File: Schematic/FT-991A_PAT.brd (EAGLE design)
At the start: 44.6 x 59.8 mm, 32 parts, among them Q2 MC78L09ABDR2GOSCT, Q5 NCP553, Q7 J310, Q8 5086, X1 IF_IN, X2 SCP_OUT, X3 SDR_OUT

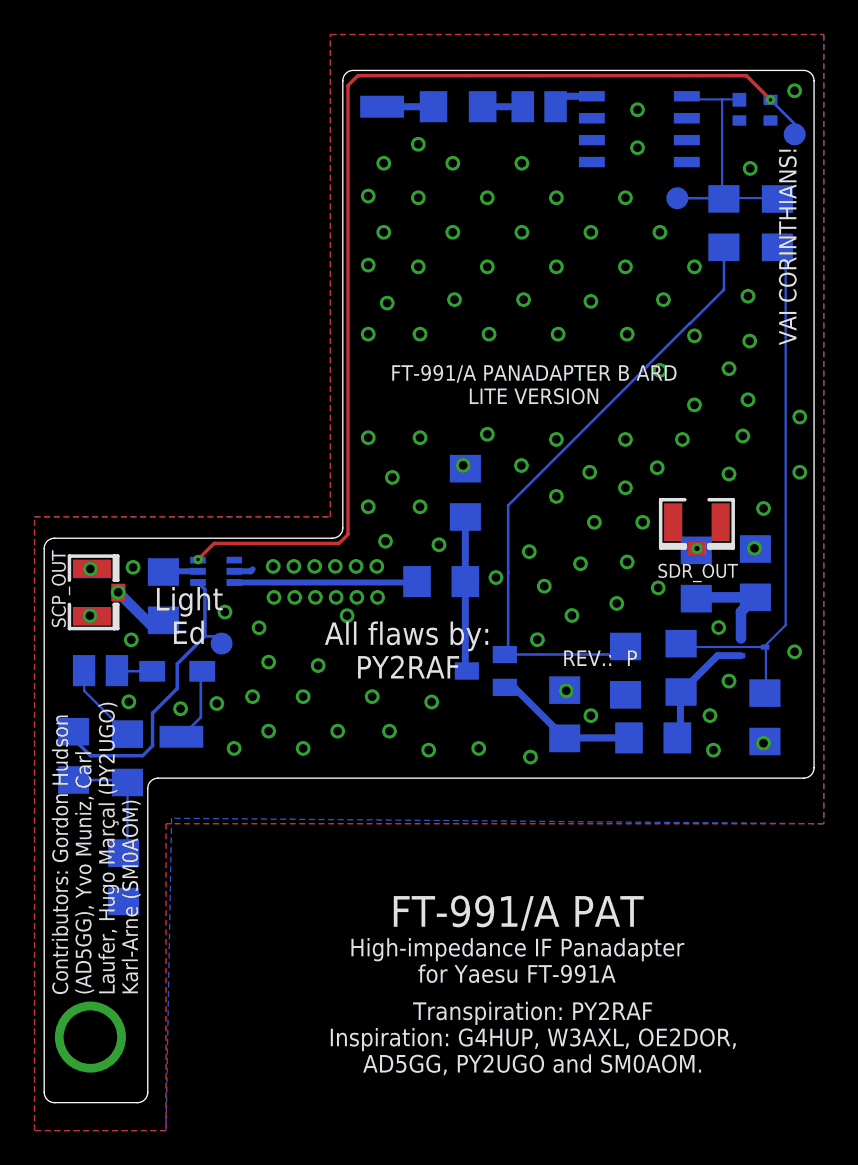
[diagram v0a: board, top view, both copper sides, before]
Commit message: Preparing: Revision Q
* Better Silk-Screen Pin 1 markings for Power regulators
* Larger footprint for 2SC5086
* Moving 0.1µF transistor caps away from RF section
* Lots of re-routing
* Changing 1 nF caps to Low ESL type and 0805 footprint for better RF
  performance
* Labeled a few signals in Eagle file for better understanding of signal
  route/path
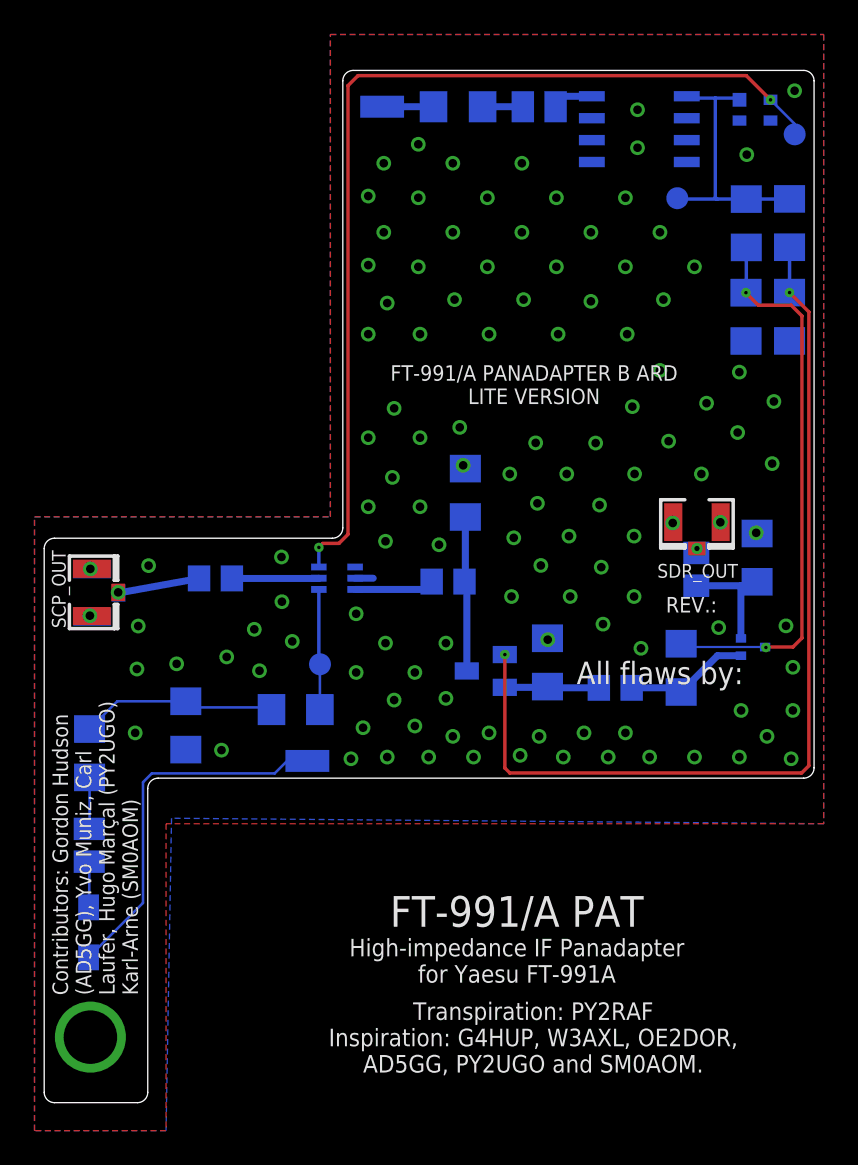
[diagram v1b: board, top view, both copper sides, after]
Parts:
- C1, C10, C13, C6: value 1nF -> 1000pF; device rcl:C3216 -> rcl:C0805
- Q1: value (none) -> PE4259
- moved C11 23.2 mm to (47.0, 57.1)
- moved C7 22.6 mm to (49.5, 57.1)
- moved D1 16.0 mm to (8.90, 21.5), turned to 270 degrees
- moved R2 13.1 mm to (20.9, 34.4), turned to 180 degrees
- moved L3 10.1 mm to (8.93, 26.5), turned to 90 degrees
- moved R4 9.51 mm to (14.5, 33.5)
- moved PAD3 7.43 mm to (21.6, 31.4)
- moved Q1 7.01 mm to (23.3, 42.0)
- moved TP3 5.82 mm to (22.3, 37.0)
- moved R6 3.80 mm to (49.5, 62.6)
- moved C10 3.64 mm to (39.4, 35.6)
- moved C1 3.19 mm to (16.2, 42.0), turned to 180 degrees
- moved R7 3.16 mm to (35.5, 37.1)
- moved R3 2.22 mm to (8.95, 31.8), turned to 270 degrees
- moved R9 1.80 mm to (47.0, 62.5)
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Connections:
- net N$10 renamed 9V5086
- net N$2 renamed IFTAP
- net N$3 renamed IFIN
- net N$37 renamed FINAL
- net N$9 renamed 9VJ310
- net VCC renamed 9V
- net VDD renamed 3V
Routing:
- net 9VJ310: track 36.1 -> 55.0 mm, vias 0 -> 2
- net N$18: track 4.30 -> 21.5 mm
- net N$7: track 17.7 -> 6.99 mm
- net 3V: track 63.2 -> 57.0 mm
- net IFIN: track 10.6 -> 4.63 mm
- net N$8: track 7.48 -> 11.6 mm
- net IFTAP: track 2.02 -> 5.05 mm
- net N$5: track 8.45 -> 5.49 mm
- net N$25: track 4.72 -> 2.99 mm
- net N$27: track 3.58 -> 4.74 mm
- net 9V5086: track 31.6 -> 32.4 mm, vias 0 -> 2
- net 9V: track 14.8 -> 15.6 mm
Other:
- board text added: "All flaws by:"
- board text added: "PY2RAF"
- board text removed: "All flaws by: PY2RAF"

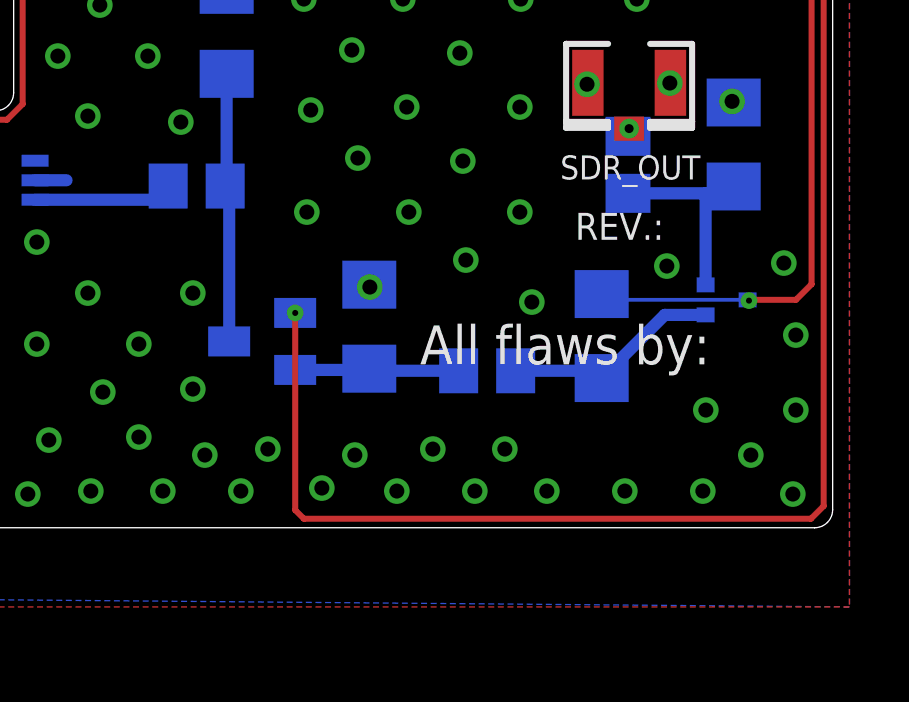
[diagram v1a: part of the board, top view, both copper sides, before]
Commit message: Minor routing hacks
- Replaced J310 JFET
  * Taking full advantage of its Source and Drain interchangeability
  * Avoiding some signal track xing
- And more routing changes.
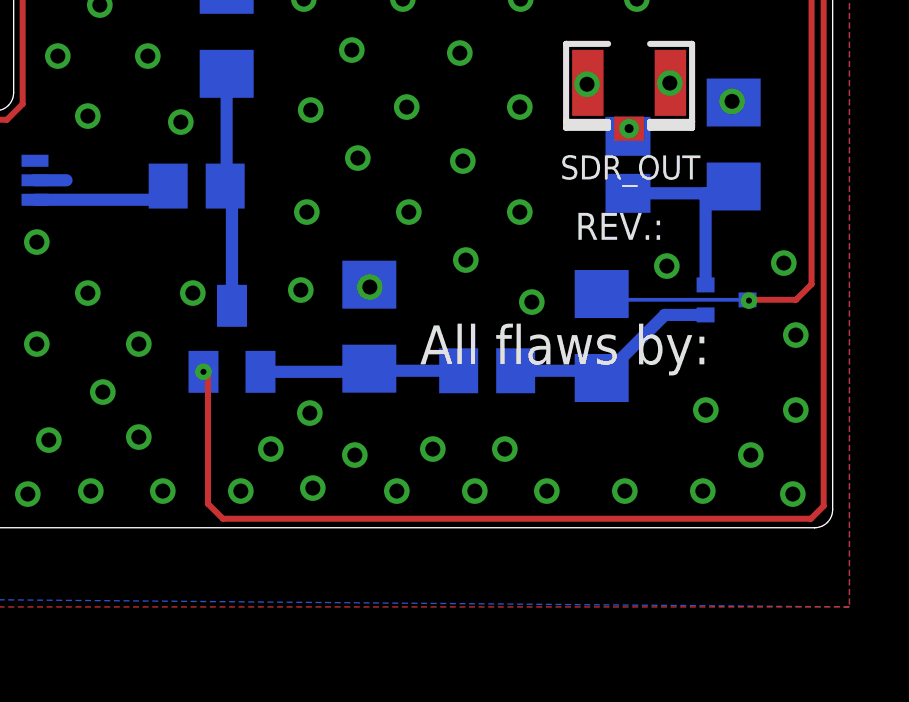
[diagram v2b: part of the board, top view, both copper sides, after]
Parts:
- Q7: device transistor-fet:SOT23 -> aarf:SOT23-3
- moved Q7 1.01 mm to (30.9, 36.7), turned to 0 degrees
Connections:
- net N$27 renamed RAWIN
- net 9VJ310: now also Q7.2; no longer Q7.1
- net N$5: now also Q7.1; no longer Q7.2
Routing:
- net N$5: track 5.49 -> 6.68 mm
- net N$6: track 9.00 -> 7.85 mm
- net 9VJ310: track 55.0 -> 55.9 mm
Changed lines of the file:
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@@
 <drawing>
 <settings>
-<setting alwaysvectorfont="no"/>
+<setting alwaysvectorfont="yes"/>
 <setting keepoldvectorfont="yes"/>
 <setting verticaltext="up"/>
@@
 <attribute name="VALUE" x="43.8775" y="57.1275" size="0.8" layer="22" font="vector" ratio="15" rot="MR270" align="top-center"/>
 </element>
-<element name="Q7" library="transistor-fet" library_urn="urn:adsk.eagle:library:396" package="SOT23" package3d_urn="urn:adsk.eagle:package:28534/2" value="J310" x="31.9075" y="36.612815625" smashed="yes" rot="MR270">
-<attribute name="SPICEPREFIX" value="J" x="31.9075" y="36.612815625" size="1.778" layer="28" rot="MR270" display="off"/>
-<attribute name="VALUE" x="31.9075" y="33.907815625" size="0.8" layer="22" font="vector" ratio="15" rot="MR180" align="top-center"/>
-</element>
 <element name="Q8" library="aarf" package="2-2H1A" value="5086" x="47.3875" y="37.9975" smashed="yes" rot="MR90">
 <attribute name="VALUE" x="47.2025" y="36.2875" size="0.8" layer="22" font="vector" ratio="15" rot="MR0" align="center"/>
@@
 <attribute name="TP_SIGNAL_NAME" value="" x="22.3" y="37" size="1.778" layer="28" rot="MR0" display="off"/>
 <attribute name="VALUE" x="22.935" y="36.238" size="0.0254" layer="28" rot="MR0"/>
+</element>
+<element name="Q7" library="aarf" package="SOT23-3" value="J310" x="30.9" y="36.7" smashed="yes" rot="MR0">
+<attribute name="VALUE" x="30.905" y="34.225" size="0.8" layer="22" font="vector" ratio="15" rot="MR0" align="center"/>
 </element>
 </elements>
@@
 <contactref element="R7" pad="2"/>
 <contactref element="C10" pad="1"/>
-<contactref element="Q7" pad="2"/>
-<wire x1="33.0075" y1="35.662815625" x2="35.435315625" y2="35.662815625" width="0.4064" layer="16"/>
-<wire x1="35.435315625" y1="35.662815625" x2="35.4775" y2="35.705" width="0.4064" layer="16"/>
+<contactref element="Q7" pad="1"/>
+<wire x1="31.85" y1="35.6" x2="35.3725" y2="35.6" width="0.4064" layer="16"/>
+<wire x1="35.3725" y1="35.6" x2="35.4775" y2="35.705" width="0.4064" layer="16"/>
 <wire x1="35.4775" y1="35.705" x2="35.5475" y2="35.635" width="0.4064" layer="16"/>
 <wire x1="35.5475" y1="35.635" x2="38.455" y2="35.635" width="0.4064" layer="16"/>
 </signal>
 <signal name="N$6">
-<contactref element="Q7" pad="3"/>
 <contactref element="R5" pad="2"/>
 <contactref element="C6" pad="2"/>
-<wire x1="30.8075" y1="41.655409375" x2="30.67225625" y2="41.790653125" width="0.4064" layer="16"/>
-<wire x1="30.8075" y1="36.612815625" x2="30.8075" y2="41.655409375" width="0.4064" layer="16"/>
 <wire x1="30.7225" y1="45.5325" x2="30.7225" y2="41.840896875" width="0.4064" layer="16"/>
 <wire x1="30.7225" y1="41.840896875" x2="30.67225625" y2="41.790653125" width="0.4064" layer="16"/>
+<contactref element="Q7" pad="3"/>
+<wire x1="30.9" y1="37.8" x2="30.9" y2="41.562909375" width="0.4064" layer="16"/>
+<wire x1="30.9" y1="41.562909375" x2="30.67225625" y2="41.790653125" width="0.4064" layer="16"/>
 </signal>
 <signal name="GNDA" airwireshidden="yes">
@@
 <via x="26.595" y="34.925" extent="1-16" drill="0.5"/>
 <via x="24.395" y="36.525" extent="1-16" drill="0.5"/>
-<via x="29.595" y="35.025" extent="1-16" drill="0.5"/>
+<via x="33.195" y="38.325" extent="1-16" drill="0.5"/>
 <via x="24.795" y="33.325" extent="1-16" drill="0.5"/>
 <via x="24.095" y="31.525" extent="1-16" drill="0.5"/>
@@
 <via x="38.995" y="31.625" extent="1-16" drill="0.5"/>
 <via x="36.395" y="31.625" extent="1-16" drill="0.5"/>
-<via x="32.095" y="33.025" extent="1-16" drill="0.5"/>
+<via x="32.195" y="33.025" extent="1-16" drill="0.5"/>
 <via x="31.195" y="31.625" extent="1-16" drill="0.5"/>
 <via x="28.595" y="31.625" extent="1-16" drill="0.5"/>
@@
 <via x="37.595" y="33.025" extent="1-16" drill="0.5"/>
 <via x="34.995" y="32.825" extent="1-16" drill="0.5"/>
-<via x="33.895" y="31.725" extent="1-16" drill="0.5"/>
-<via x="29.995" y="32.825" extent="1-16" drill="0.5"/>
+<via x="33.595" y="31.725" extent="1-16" drill="0.5"/>
+<via x="33.495" y="34.225" extent="1-16" drill="0.5"/>
 <via x="27.795" y="33.425" extent="1-16" drill="0.5"/>
 <via x="39.995" y="33.025" extent="1-16" drill="0.5"/>
@@
 <signal name="9VJ310">
 <contactref element="R6" pad="1"/>
-<contactref element="Q7" pad="1"/>
 <contactref element="C7" pad="1"/>
-<wire x1="33" y1="37.570315625" x2="33.0075" y2="37.562815625" width="0.2" layer="16"/>
 <via x="49.5025" y="58.5325" extent="1-16" drill="0.2"/>
 <wire x1="49.5025" y1="58.5325" x2="50.6225" y2="57.4125" width="0.2" layer="1"/>
-<wire x1="50.2" y1="30.7025" x2="50.6225" y2="31.125" width="0.2" layer="1"/>
+<wire x1="50.6225" y1="31.125" x2="50.2" y2="30.7025" width="0.2" layer="1"/>
 <wire x1="50.6225" y1="57.4125" x2="50.6225" y2="31.125" width="0.2" layer="1"/>
-<via x="33.0075" y="37.562815625" extent="1-16" drill="0.2"/>
-<wire x1="33.0075" y1="37.562815625" x2="33.0075" y2="30.9925" width="0.2" layer="1"/>
-<wire x1="33.0075" y1="30.9925" x2="33.2975" y2="30.7025" width="0.2" layer="1"/>
-<wire x1="33.2975" y1="30.7025" x2="50.2" y2="30.7025" width="0.2" layer="1"/>
 <wire x1="49.5025" y1="61.16" x2="49.5025" y2="58.5325" width="0.2" layer="16"/>
+<contactref element="Q7" pad="2"/>
+<wire x1="30.5975" y1="30.7025" x2="50.2" y2="30.7025" width="0.2" layer="1"/>
+<wire x1="30.5975" y1="30.7025" x2="30.1" y2="31.2" width="0.2" layer="1"/>
+<wire x1="30.1" y1="31.2" x2="30.1" y2="33.9" width="0.2" layer="1"/>
+<wire x1="30.1" y1="33.9" x2="30.1" y2="34.05" width="0.2" layer="1"/>
+<wire x1="30.1" y1="34.05" x2="30.1" y2="35.45" width="0.2" layer="1"/>
+<wire x1="30.1" y1="35.45" x2="29.95" y2="35.6" width="0.2" layer="1"/>
+<via x="29.95" y="35.6" extent="1-16" drill="0.2"/>
 </signal>
 <signal name="9V5086">
@@
 <wire x1="49.8" y1="68.3" x2="48.4" y2="69.7" width="0.1524" layer="16"/>
 </signal>
-<signal name="N$27">
+<signal name="RAWIN">
 <contactref element="C1" pad="1"/>
 <contactref element="X1" pad="3"/>

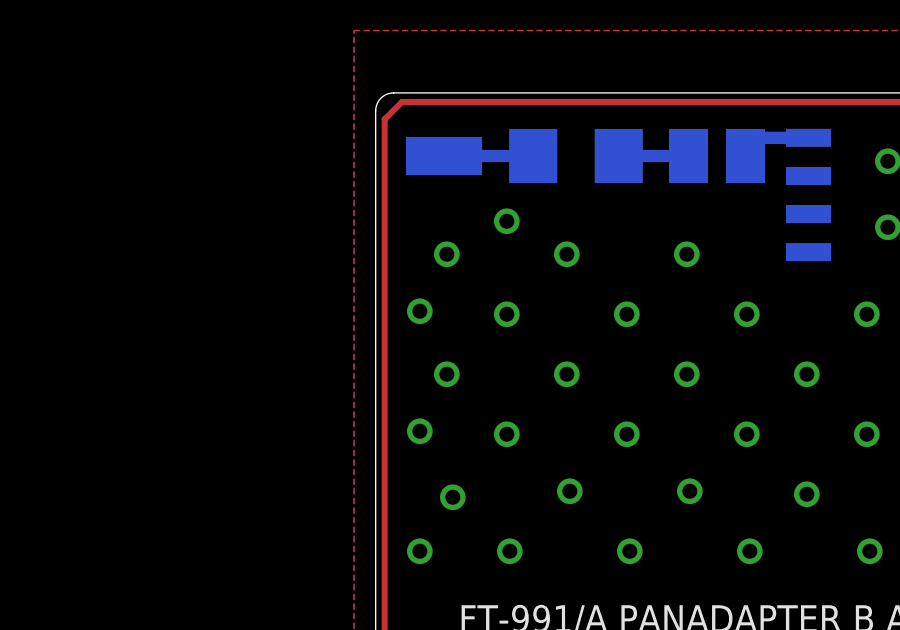
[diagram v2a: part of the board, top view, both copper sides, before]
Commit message: Rev. Q more enhancements
- Changed two resistors in Amplifier chain in order to get some more
  gain - See Issue 14
- Updated BOM in order to reflect this change
- Added a ground pad, that's useful when troubleshooting and the lack
  of it bit my butt a number of times
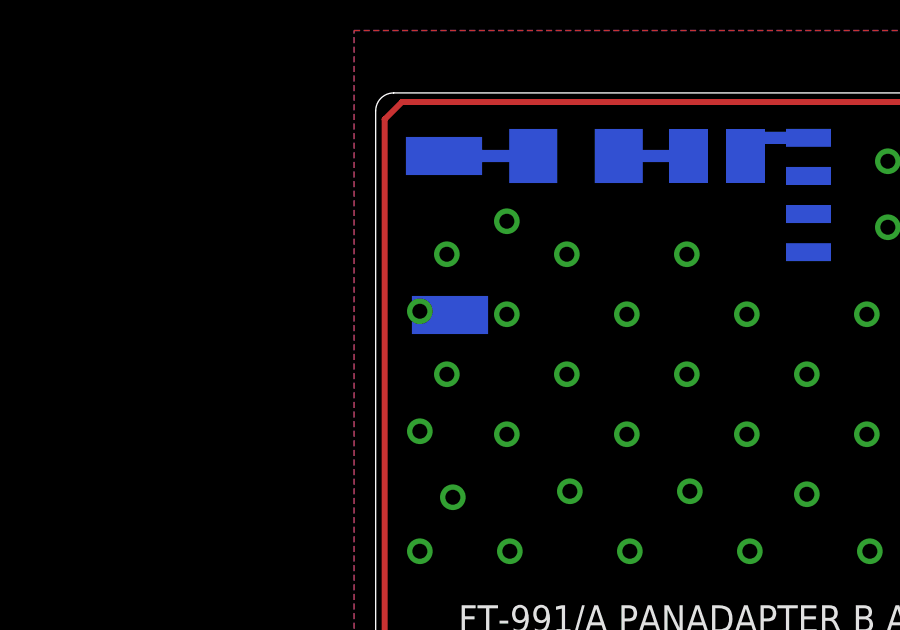
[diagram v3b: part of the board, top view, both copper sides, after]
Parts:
- added GND: GND, wirepad:SMD1,27-2,54
- R10: value 100Ω -> 220Ω
- R8: value 39kΩ -> 10kΩ
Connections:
- net GNDA: now also GND.1
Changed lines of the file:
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@@
 <drawing>
 <settings>
-<setting alwaysvectorfont="yes"/>
+<setting alwaysvectorfont="no"/>
 <setting keepoldvectorfont="yes"/>
 <setting verticaltext="up"/>
@@
 <attribute name="VALUE" x="45.3625" y="62.525" size="0.8" layer="22" font="vector" ratio="15" rot="MR90" align="center"/>
 </element>
-<element name="R8" library="rcl" library_urn="urn:adsk.eagle:library:334" package="R3216" package3d_urn="urn:adsk.eagle:package:23557/2" value="39kΩ" x="43.2225" y="36.7925" smashed="yes" rot="MR270">
+<element name="R8" library="rcl" library_urn="urn:adsk.eagle:library:334" package="R3216" package3d_urn="urn:adsk.eagle:package:23557/2" value="10kΩ" x="43.2225" y="36.7925" smashed="yes" rot="MR270">
 <attribute name="SPICEPREFIX" value="R" x="43.2225" y="36.7925" size="1.778" layer="28" rot="MR270" display="off"/>
 <attribute name="VALUE" x="43.2275" y="33.9375" size="0.8" layer="22" font="vector" ratio="15" rot="MR0" align="top-center"/>
 </element>
-<element name="R10" library="rcl" library_urn="urn:adsk.eagle:library:334" package="R3216" package3d_urn="urn:adsk.eagle:package:23557/2" value="100Ω" x="47.6225" y="43.1775" smashed="yes" rot="MR90">
+<element name="R10" library="rcl" library_urn="urn:adsk.eagle:library:334" package="R3216" package3d_urn="urn:adsk.eagle:package:23557/2" value="220Ω" x="47.6225" y="43.1775" smashed="yes" rot="MR90">
 <attribute name="SPICEPREFIX" value="R" x="47.6225" y="43.1775" size="1.778" layer="28" rot="MR90" display="off"/>
 <attribute name="VALUE" x="49.7825" y="43.2425" size="0.8" layer="22" font="vector" ratio="15" rot="MR90" align="top-center"/>
@@
 <element name="Q7" library="aarf" package="SOT23-3" value="J310" x="30.9" y="36.7" smashed="yes" rot="MR0">
 <attribute name="VALUE" x="30.905" y="34.225" size="0.8" layer="22" font="vector" ratio="15" rot="MR0" align="center"/>
+</element>
+<element name="GND" library="wirepad" library_urn="urn:adsk.eagle:library:412" package="SMD1,27-2,54" package3d_urn="urn:adsk.eagle:package:30839/1" value="GND" x="26.1" y="64" smashed="yes" rot="MR270">
+<attribute name="NAME" x="28" y="62.4" size="0.8" layer="22" font="vector" ratio="15" rot="MR0" align="center"/>
+<attribute name="VALUE" x="9.3" y="53.8" size="0.0254" layer="28" rot="MR270"/>
 </element>
 </elements>
@@
 <via x="40.895" y="37.925" extent="1-16" drill="0.5"/>
 <via x="20.695" y="38.325" extent="1-16" drill="0.5"/>
+<contactref element="GND" pad="1"/>
 <wire x1="24.395" y1="39.925" x2="24.335" y2="41.985" width="0" layer="19" extent="16-16"/>
 <wire x1="8.995" y1="42.525" x2="9.08411875" y2="42.541790625" width="0" layer="19" extent="1-1"/>
